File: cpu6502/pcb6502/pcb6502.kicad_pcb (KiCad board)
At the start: 2 copper layers, 134.6 x 134.6 mm, 41 parts, among them J1 Power, J2 RS232, J6 Address, J7 Data, J8 CPU, SW1 Reset, SW2 IRQ Enable, SW3 Debug, U1 6502 (CPU), U2 28C256 (ROM)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

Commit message: checkpoint, most significantly OS works!!
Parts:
- added D5: Activity, LED_THT:LED_D5.0mm, F.Cu at (108.0, 109.2)
- added D6: 1N5819, Diode_THT:D_DO-41_SOD81_P10.16mm_Horizontal, F.Cu at (182.9, 25.4)
- added J3: 5v Power, TerminalBlock_TE-Connectivity:TerminalBlock_TE_282834-2_1x02_P2.54mm_Horizontal, F.Cu at (165.1, 24.1)
- added R6: 220, Resistor_THT:R_Axial_DIN0204_L3.6mm_D1.6mm_P7.62mm_Horizontal, F.Cu at (114.3, 110.5)
- D1: value Power LED -> Power
- D4: value Rec -> Receive; footprint LED_THT:LED_D3.0mm -> LED_THT:LED_D5.0mm
- J2: footprint Connector_Dsub:DSUB-9_Female_Horizontal_P2.77x2.54mm_EdgePinOffset9.40mm -> Connector_Dsub:DSUB-9_Male_Horizontal_P2.77x2.84mm_EdgePinOffset4.94mm_Housed_MountingHolesOffset7.48mm
- R1: footprint Resistor_THT:R_Axial_DIN0207_L6.3mm_D2.5mm_P2.54mm_Vertical -> Resistor_THT:R_Axial_DIN0204_L3.6mm_D1.6mm_P7.62mm_Horizontal
- R5: footprint Resistor_THT:R_Axial_DIN0204_L3.6mm_D1.6mm_P2.54mm_Vertical -> Resistor_THT:R_Axial_DIN0204_L3.6mm_D1.6mm_P7.62mm_Horizontal
- U3: value 62256 RAM -> 62256 (RAM)
- moved R1 86.8 mm to (114.3, 106.7)
- moved D4 70.4 mm to (127.0, 109.2), turned to 0 degrees
- moved C6 19.4 mm to (196.8, 110.5), turned to 90 degrees
- moved J2 15.6 mm to (197.6, 75.0)
- moved C4 11.4 mm to (195.6, 92.7)
- moved C5 10.2 mm to (193.1, 96.5)
- moved R5 9.25 mm to (185.4, 125.7), turned to 90 degrees
- moved C3 3.81 mm to (195.6, 100.3)
- moved C2 2.54 mm to (195.5, 104.1)
- moved SW3 2.54 mm to (189.8, 119.7)
- moved J1 1.31 mm to (190.8, 34.3)
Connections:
- U4 pad 18: /CB1 -> unconnected-(U4-CB1-Pad18)
- U4 pad 19: /CB2 -> unconnected-(U4-CB2-Pad19)
- U4 pad 3: /PA1 -> unconnected-(U4-PA1-Pad3)
- U4 pad 39: /CA2 -> unconnected-(U4-CA2-Pad39)
- U4 pad 4: /PA2 -> unconnected-(U4-PA2-Pad4)
- U4 pad 5: /PA3 -> unconnected-(U4-PA3-Pad5)
- U4 pad 6: /PA4 -> unconnected-(U4-PA4-Pad6)
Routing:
- net Net-(D4-A): track 39.8 -> 102.5 mm, vias 1 -> 2
- net GND: track 52.8 -> 19.6 mm, vias 2 -> 1
- net /PA0: track 0.00 -> 31.1 mm
- net +5V: track 576.7 -> 591.3 mm
- net Net-(D5-K): track 0.00 -> 7.93 mm
- net Net-(D4-K): track 6.13 -> 13.8 mm
- net Net-(D6-A): track 0.00 -> 5.61 mm
- net Net-(D3-A): track 25.1 -> 19.7 mm
- net /PA5: track 57.9 -> 62.9 mm
- net Net-(U8-T1OUT): track 38.9 -> 34.2 mm, vias 0 -> 1
- net /232_VS+: track 22.2 -> 18.0 mm
- net /PA6: track 60.5 -> 64.5 mm
- net Net-(U8-C2-): track 9.22 -> 12.4 mm
- net Net-(U8-C2+): track 11.6 -> 14.6 mm
- net /PB7: track 90.9 -> 93.9 mm
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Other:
- board text added: "+"
- board text added: "Power 6-12v (center +)"
- board text added: "RS232 - 19200 Baud 8 data bits, 1 Stop Bit No Parity, CR only UPPER case only"
- board text removed: "Power 6-12v Input (center +)"

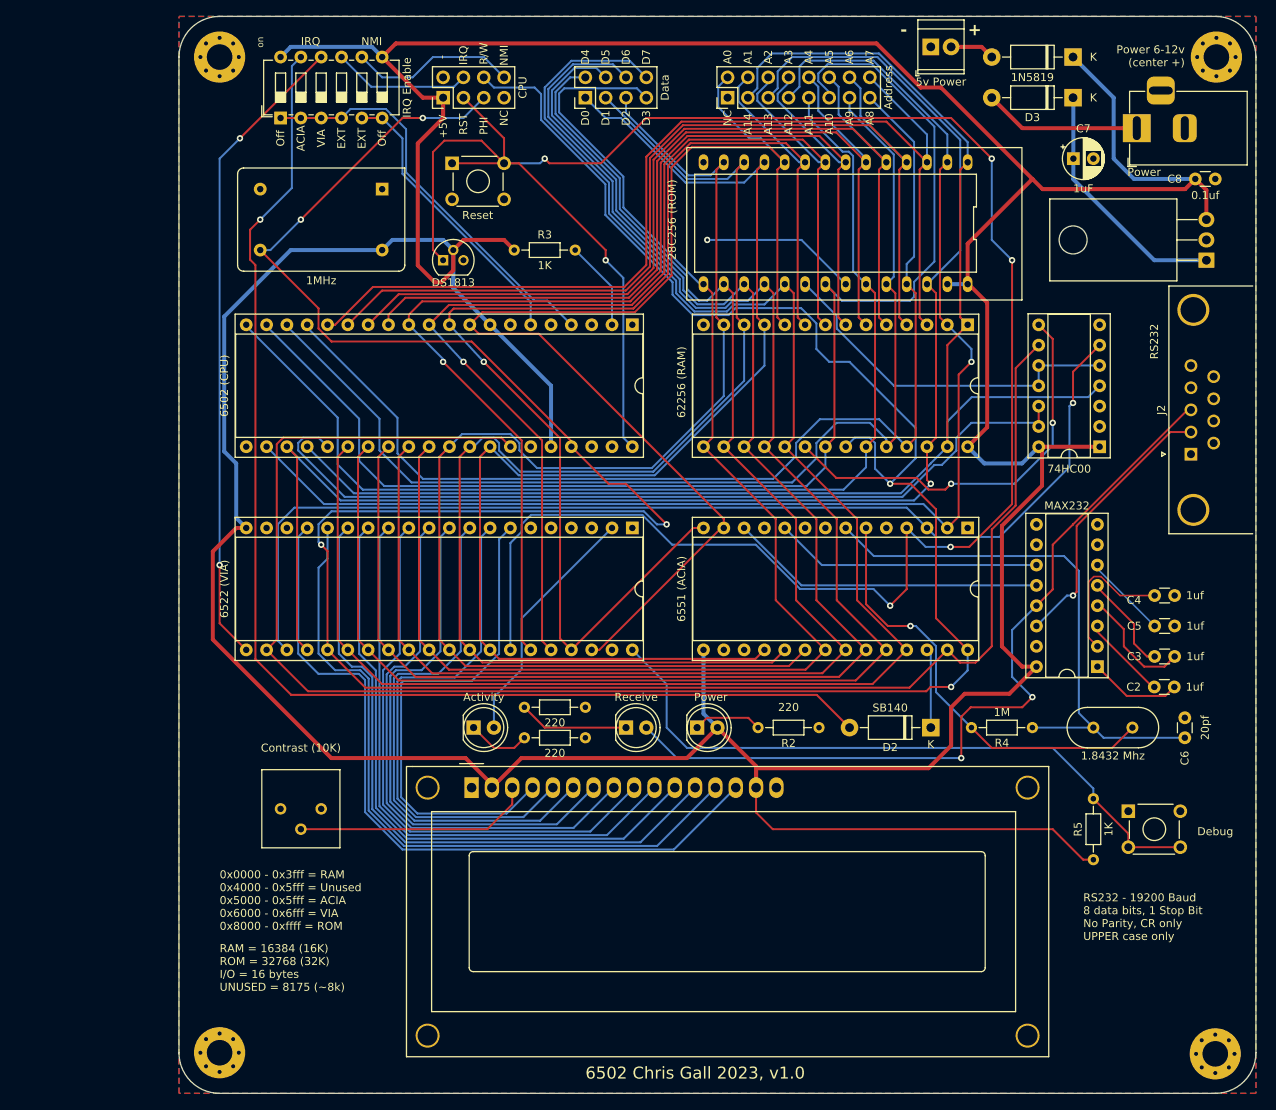
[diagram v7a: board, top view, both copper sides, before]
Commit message: PCB 99.9999% ready to be built (without LCD)
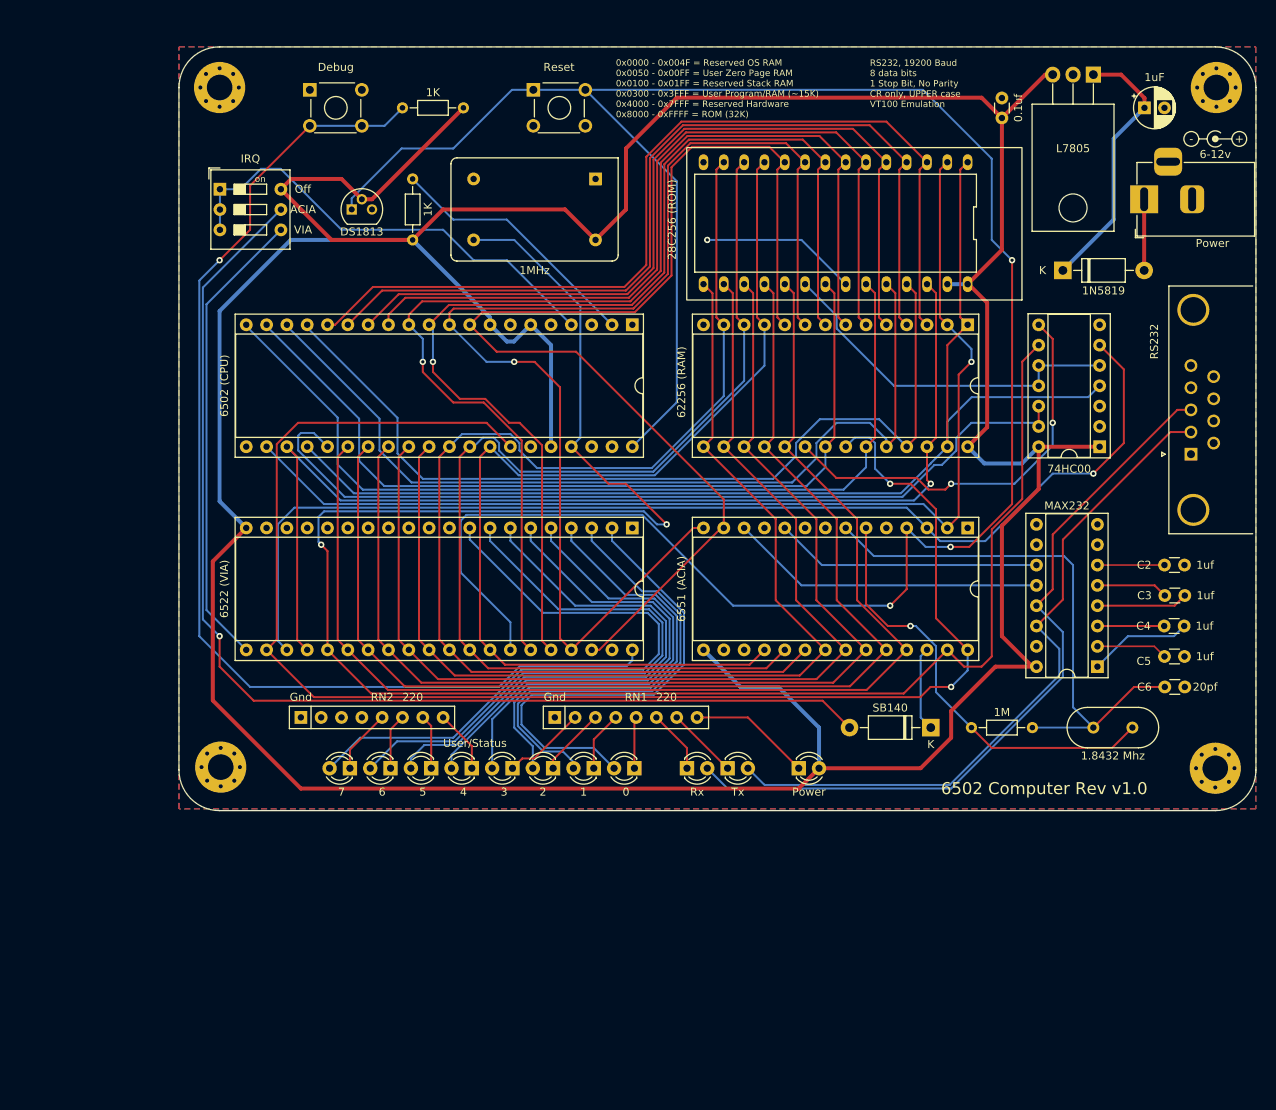
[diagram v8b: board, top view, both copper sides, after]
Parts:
- removed DS1: HY1602E, Display:WC1602A
- removed J3: 5v Power, TerminalBlock_TE-Connectivity:TerminalBlock_TE_282834-2_1x02_P2.54mm_Horizontal
- removed J6: Address, Connector_PinHeader_2.54mm:PinHeader_2x08_P2.54mm_Vertical
- removed J7: Data, Connector_PinHeader_2.54mm:PinHeader_2x04_P2.54mm_Vertical
- removed J8: CPU, Connector_PinHeader_2.54mm:PinHeader_2x04_P2.54mm_Vertical
- removed R1, R2, R6: 220, Resistor_THT:R_Axial_DIN0204_L3.6mm_D1.6mm_P7.62mm_Horizontal
- removed RV1: Contrast (10K), Potentiometer_THT:Potentiometer_Bourns_3386P_Vertical
- added D10: 4, LED_THT:LED_D3.0mm, F.Cu at (107.7, 114.3)
- added D11: 5, LED_THT:LED_D3.0mm, F.Cu at (102.7, 114.3)
- added D12: 6, LED_THT:LED_D3.0mm, F.Cu at (97.6, 114.3)
- added D13: 7, LED_THT:LED_D3.0mm, F.Cu at (92.5, 114.3)
- added D7: Tx, LED_THT:LED_D3.0mm, F.Cu at (139.7, 114.3)
- added D8: 2, LED_THT:LED_D3.0mm, F.Cu at (117.9, 114.3)
- added D9: 3, LED_THT:LED_D3.0mm, F.Cu at (112.8, 114.3)
- added REF**: 6-12v, Symbol:Symbol_Barrel_Polarity, F.Cu at (200.7, 35.6)
- added RN1: 220, Resistor_THT:R_Array_SIP8, F.Cu at (118.1, 108.0)
- added RN2: 220, Resistor_THT:R_Array_SIP8, F.Cu at (86.4, 108.0)
- D1: footprint LED_THT:LED_D5.0mm -> LED_THT:LED_D3.0mm
- D4: value Receive -> Rx; footprint LED_THT:LED_D5.0mm -> LED_THT:LED_D3.0mm
- D5: value Activity -> 0; footprint LED_THT:LED_D5.0mm -> LED_THT:LED_D3.0mm
- D6: value 1N5819 -> 1; footprint Diode_THT:D_DO-41_SOD81_P10.16mm_Horizontal -> LED_THT:LED_D3.0mm
- SW2: value IRQ Enable -> IRQ; footprint Button_Switch_THT:SW_DIP_SPSTx06_Slide_6.7x16.8mm_W7.62mm_P2.54mm_LowProfile -> Button_Switch_THT:SW_DIP_SPSTx03_Slide_9.78x9.8mm_W7.62mm_P2.54mm
- moved SW3 136.4 mm to (87.5, 29.5)
- moved R5 122.6 mm to (106.7, 31.8), turned to 180 degrees
- moved D6 107.2 mm to (123.0, 114.3)
- moved H3 35.7 mm to (76.3, 114.2)
- moved H4 35.7 mm to (200.7, 114.3)
- moved U6 27.2 mm to (185.4, 27.6), turned to 180 degrees
- moved X1 26.7 mm to (123.2, 40.6)
- moved C8 25.3 mm to (174.0, 33.0), turned to 90 degrees
- moved D3 21.6 mm to (181.6, 52.1), turned to 0 degrees
- moved D5 20.7 mm to (128.1, 114.3), turned to 180 degrees
- moved SW1 13.7 mm to (115.4, 29.5)
- moved D1 13.7 mm to (148.6, 114.3)
- moved U9 13.1 mm to (92.7, 44.5)
- moved R3 12.8 mm to (100.3, 48.3), turned to 90 degrees
- moved SW2 11.7 mm to (76.2, 41.9), turned to 0 degrees
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- renumbered C5 to C2, C2 to C4, C4 to C5
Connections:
- net Net-(D4-A) renamed /232_RX
- net Net-(U8-T1OUT) renamed /232_TX
- D1 pad 1: Net-(D1-K) -> /RNPA0
- D4 pad 1: Net-(D4-K) -> /RNPA2
- D5 pad 1: Net-(D5-K) -> /RNPA3
- D6 pad 1: +5V -> /RNPA4
- D6 pad 2: Net-(D6-A) -> /PA1
- SW2 pad 4: /IRQ -> /VIAIRQ
- SW2 pad 5: /NMI -> /ACIAIRQ
- SW2 pad 6: /NMI -> +5V
- U1 pad 6: /NMI -> +5V
- U4 pad 10: /PB0 -> unconnected-(U4-PB0-Pad10)
- U4 pad 11: /PB1 -> unconnected-(U4-PB1-Pad11)
- U4 pad 12: /PB2 -> unconnected-(U4-PB2-Pad12)
- U4 pad 13: /PB3 -> unconnected-(U4-PB3-Pad13)
- U4 pad 14: /PB4 -> unconnected-(U4-PB4-Pad14)
- U4 pad 15: /PB5 -> unconnected-(U4-PB5-Pad15)
- U4 pad 16: /PB6 -> unconnected-(U4-PB6-Pad16)
- U4 pad 17: /PB7 -> unconnected-(U4-PB7-Pad17)
- U4 pad 3: unconnected-(U4-PA1-Pad3) -> /PA1
- U4 pad 4: unconnected-(U4-PA2-Pad4) -> /PA2
- U4 pad 5: unconnected-(U4-PA3-Pad5) -> /PA3
- U4 pad 6: unconnected-(U4-PA4-Pad6) -> /PA4
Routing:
- net /PB7: track 93.9 -> 0.00 mm
- net +5V: track 591.3 -> 500.4 mm
- net /PB6: track 88.4 -> 0.00 mm
- net /R/W: track 274.3 -> 188.4 mm
- net /PB5: track 83.0 -> 0.00 mm
- net /PB4: track 77.9 -> 0.00 mm
- net /PB3: track 73.6 -> 0.00 mm
- net /PB2: track 71.0 -> 0.00 mm
- net /PB1: track 69.1 -> 0.00 mm
- net /PB0: track 67.6 -> 0.00 mm
- net /D7: track 216.2 -> 153.4 mm
- net /PA4: track 0.00 -> 61.9 mm
- net /PA3: track 0.00 -> 58.0 mm
- net /CA1: track 83.6 -> 141.5 mm, vias 0 -> 1
- net /PA1: track 0.00 -> 57.4 mm
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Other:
- board size 134.6 x 134.6 mm -> 134.6 x 95.5 mm
- board text added: "0x0000 - 0x004F = Reserved OS RAM 0x0050 - 0x00FF = User Zero Page RAM 0x0100 - 0x01FF = Reserved Stack RAM 0x0300 - 0x3FFF = User Program/RAM (~15K) 0x4000 - 0x7FFF = Reserved Hardware 0x8000 - 0xFFFF = ROM (32K)"
- board text added: "6502 Computer Rev v1.0"
- board text added: "Gnd"
- board text added: "RS232, 19200 Baud 8 data bits 1 Stop Bit, No Parity CR only, UPPER case VT100 Emulation"
- board text added: "User/Status"
- board text removed: "+5V"
- board text removed: "0x0000 - 0x3fff = RAM 0x4000 - 0x5fff = Unused 0x5000 - 0x5fff = ACIA 0x6000 - 0x6fff = VIA 0x8000 - 0xffff = ROM"
- board text removed: "6502 Chris Gall 2023, v1.0"
- board text removed: "A0"
- board text removed: "A1"
- board text removed: "A10"
- board text removed: "A11"
- board text removed: "A12"
- board text removed: "A13"
- board text removed: "A14"
- board text removed: "A2"
- board text removed: "A3"
- board text removed: "A4"
- board text removed: "A5"
- board text removed: "A6"
- board text removed: "A7"
- board text removed: "A8"
- board text removed: "A9"
- board text removed: "D0"
- board text removed: "D1"
- board text removed: "D2"
- board text removed: "D3"
- board text removed: "D4"
- board text removed: "D5"
- board text removed: "D6"
- board text removed: "D7"
- board text removed: "EXT"
- board text removed: "IRQ"
- board text removed: "NC"
- board text removed: "NMI"
- board text removed: "PHI"
- board text removed: "Power 6-12v (center +)"
- board text removed: "R/W"
- board text removed: "RAM = 16384 (16K) ROM = 32768 (32K) I/O = 16 bytes UNUSED = 8175 (~8k)"
- board text removed: "RS232 - 19200 Baud 8 data bits, 1 Stop Bit No Parity, CR only UPPER case only"
- board text removed: "RST"
